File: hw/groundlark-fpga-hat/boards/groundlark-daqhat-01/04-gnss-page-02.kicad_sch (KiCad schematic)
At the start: 1 part

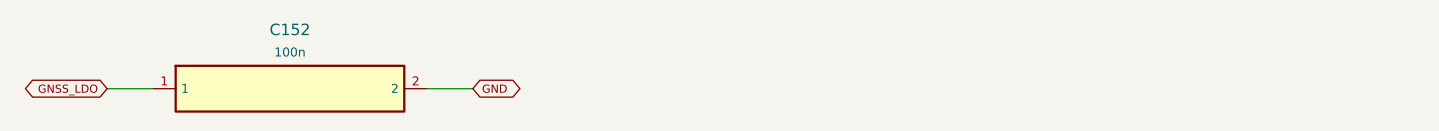
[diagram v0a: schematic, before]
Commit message: Fix GNSS RF margin and broaden pressure filter robustness
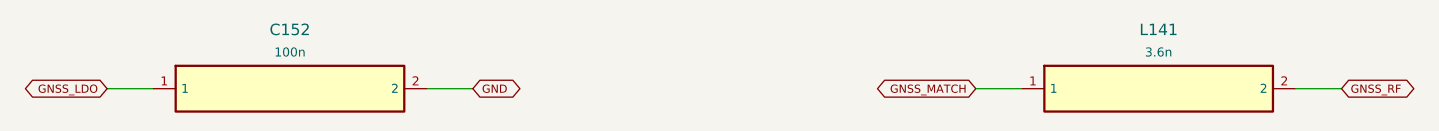
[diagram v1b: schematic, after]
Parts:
- added L141: 3.6n, Groundlark:GNSS_HP0402, symbol Groundlark:Part_L141
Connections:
- new net GNSS_MATCH: L141.1
- new net GNSS_RF: L141.2
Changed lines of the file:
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@@
 (wire (pts (xy 66.04 38.1) (xy 71.12 38.1)) (stroke (width 0) (type default)))
 (global_label "GND" (shape bidirectional) (at 71.12 38.1 0) (effects (font (size 0.9 0.9)) (justify left)))
+(symbol (lib_id "Groundlark:Part_L141") (at 147.32 38.1 0) (unit 1) (in_bom yes) (on_board yes) (dnp no)
+              (property "Reference" "L141" (at 147.32 31.560000000000002 0) (effects (font (size 1.27 1.27))))
+              (property "Value" "3.6n" (at 147.32 34.06 0) (effects (font (size 1.0 1.0))))
+              (property "Footprint" "Groundlark:GNSS_HP0402" (at 147.32 38.1 0) (effects (font (size 1 1)) hide))
+              (property "MPN" "0402HP-3N6XJRW" (at 147.32 38.1 0) (effects (font (size 1 1)) hide))
+              (instances (project "groundlark-daqhat-01" (path "/de5c43d7-546f-5b4d-b587-d8dfceb38170/d69ce701-722b-51da-9948-1c6ac928ecf5" (reference "L141") (unit 1)))))
+(wire (pts (xy 132.08 38.1) (xy 127.0 38.1)) (stroke (width 0) (type default)))
+(global_label "GNSS_MATCH" (shape bidirectional) (at 127.0 38.1 180) (effects (font (size 0.9 0.9)) (justify right)))
+(wire (pts (xy 162.56 38.1) (xy 167.64 38.1)) (stroke (width 0) (type default)))
+(global_label "GNSS_RF" (shape bidirectional) (at 167.64 38.1 0) (effects (font (size 0.9 0.9)) (justify left)))
 )
